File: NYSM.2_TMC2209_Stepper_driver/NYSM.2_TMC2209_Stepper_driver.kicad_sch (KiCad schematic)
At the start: 17 parts, among them U1 TMC2209

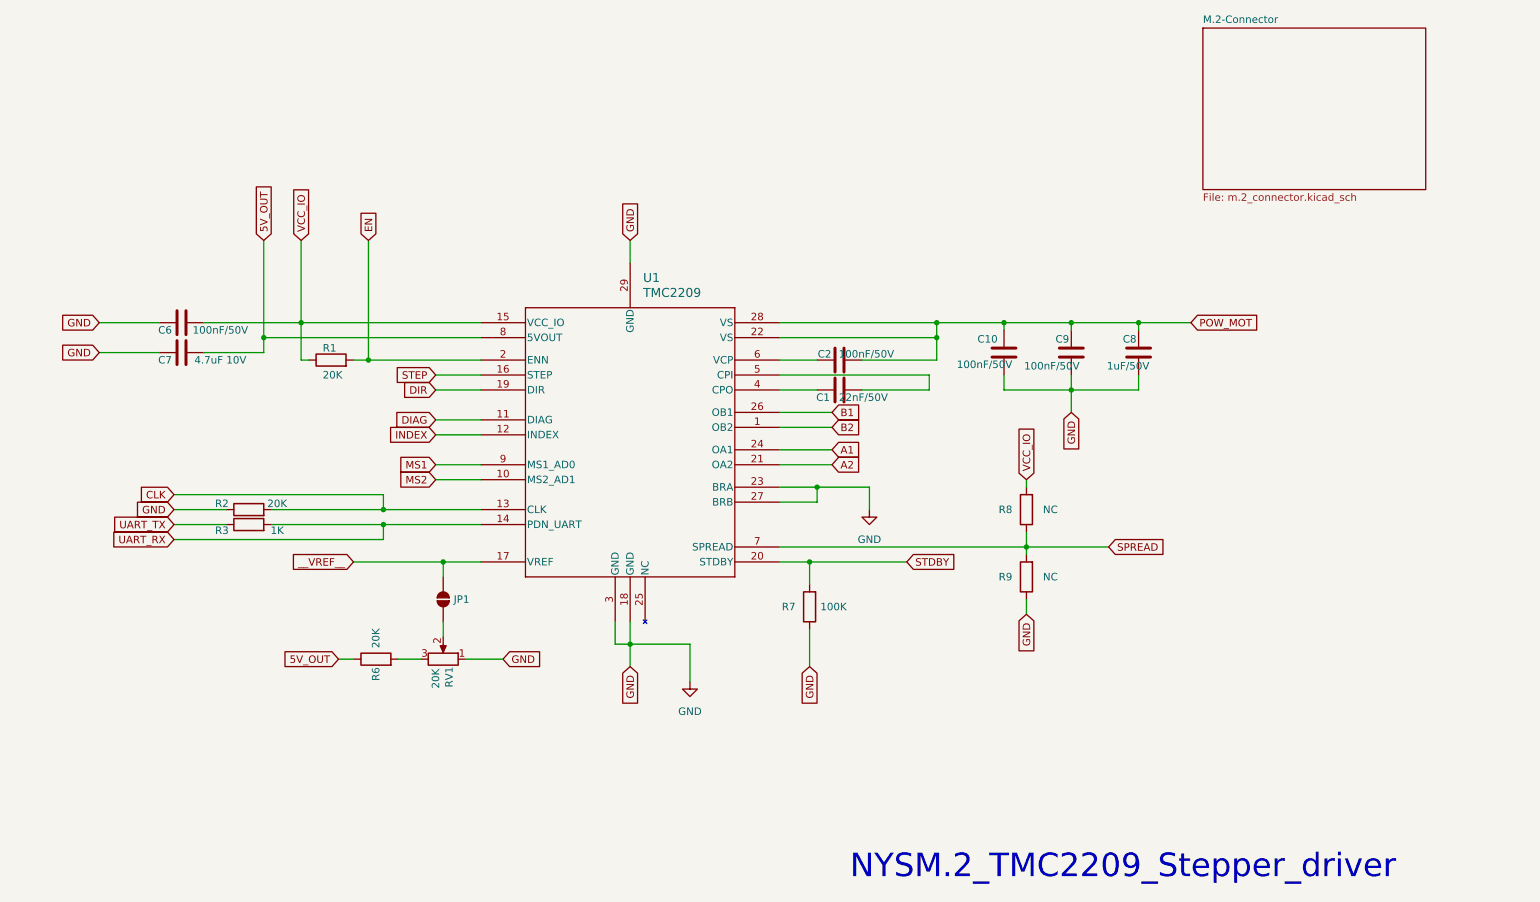
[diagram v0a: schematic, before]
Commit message: Preliminary push for alternative version with External Sense Resistors
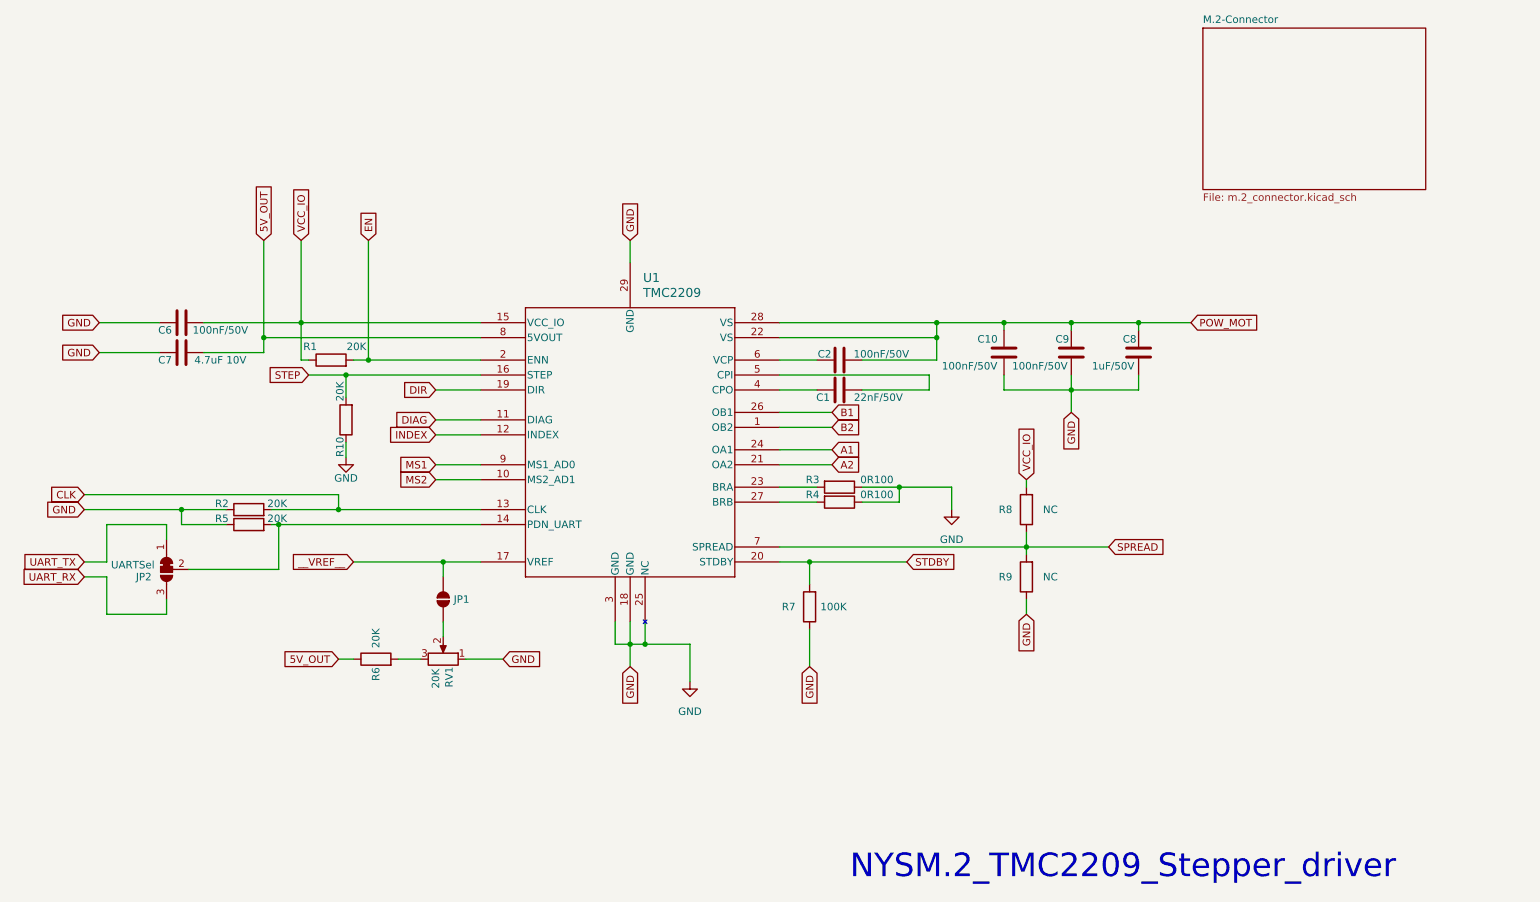
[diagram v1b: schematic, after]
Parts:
- added JP2: UARTSel, Jumper:SolderJumper-3_P1.3mm_Bridged12_RoundedPad1.0x1.5mm, symbol Jumper:SolderJumper_3_Bridged12
- added R10, R5: 20K, Resistor_SMD:R_0402_1005Metric, symbol Device:R
- added R4: 0R100, Resistor_SMD:R_1206_3216Metric, symbol Device:R
- R3: value 1K -> 0R100; footprint Resistor_SMD:R_0402_1005Metric -> Resistor_SMD:R_1206_3216Metric; LCSC# C163815 -> C3033268; Manufacturer_Part_Number WR04X1001FTL -> PT1206FR-7W0R1L
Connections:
- net GND: now also R3.1, U1.25 (NC), R10.1, R4.1, R5.1; no longer U1.23 (BRA), U1.27 (BRB)
- net STEP: now also R10.2
- net UART_RX: now also JP2.3 (B); no longer R3.2, U1.14 (PDN_UART)
- net UART_TX: now also JP2.1 (A); no longer R3.1
- new net: R3.2, U1.23 (BRA)
- new net: JP2.2 (C), R5.2, U1.14 (PDN_UART)
- new net: R4.2, U1.27 (BRB)
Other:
- title: NYSM.2 TMC2209 Module -> NYSM.2 TMC2209 Module with External Sense Resistors

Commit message: Added production Files
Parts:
- R8, R9: now not fitted
- RV1: value 20K -> 20K POT
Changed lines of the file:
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@@
 			)
 		)
-		(property "Value" "20K"
+		(property "Value" "20K POT"
 			(at 110.49 139.192 0)
 			(effects
@@
 		(in_bom yes)
 		(on_board yes)
-		(dnp no)
+		(dnp yes)
 		(property "Reference" "R9"
 			(at 207.264 121.92 0)
@@
 		(in_bom yes)
 		(on_board yes)
-		(dnp no)
+		(dnp yes)
 		(property "Reference" "R8"
 			(at 207.264 110.49 0)
